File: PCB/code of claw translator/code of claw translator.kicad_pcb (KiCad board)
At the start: 2 copper layers, 43 parts, among them J1 Conn_01x20_Socket, J10 Conn_01x01_Socket, J11 Conn_01x03_Socket, J12 Conn_01x01_Socket, J13 Conn_01x01_Socket, J14 Conn_01x01_Socket, J15 Conn_01x01_Socket, J16 Conn_01x01_Socket, J17 Conn_01x01_Socket, J18 Conn_01x01_Socket, J19 Conn_01x01_Socket, J2 Conn_01x20_Socket, J20 Conn_01x01_Socket, J21 Conn_01x01_Socket, J22 Conn_01x01_Socket, J23 Conn_01x01_Socket, J24 Conn_01x01_Socket, J25 Conn_01x01_Socket, J26 Conn_01x01_Socket, J27 Conn_01x01_Socket, J3 Conn_01x14_Socket, J32 Conn_01x01_Socket, J33 Conn_01x01_Socket, J34 Conn_01x01_Socket, J35 Conn_01x01_Socket, J36 Conn_01x01_Socket, J37 Conn_01x01_Socket, J38 Conn_01x01_Socket, J39 Conn_01x01_Socket, J4 Conn_01x08_Socket, J40 Conn_01x01_Socket, J41 Conn_01x01_Socket, J42 Conn_01x01_Socket, J43 Conn_01x01_Socket, J5 Conn_01x08_Socket, J6 Conn_01x06_Socket, J7 Conn_01x01_Socket, J8 Conn_01x01_Socket, J9 Conn_01x01_Socket

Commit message: Finished rough draft of components in PCB. Now need to wire them up.
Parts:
- removed J34, J35, J38, J39, J42, J43: Conn_01x01_Socket, Connector_PinSocket_2.54mm:PinSocket_1x01_P2.54mm_Horizontal
- J6: footprint Connector_PinSocket_2.54mm:PinSocket_1x06_P2.54mm_Horizontal -> Connector_PinSocket_2.54mm:PinSocket_1x06_P2.54mm_Vertical
- moved J7 124.2 mm to (68.2, 77.0)
- moved J25 123.5 mm to (77.9, 153.3)
- moved J24 123.4 mm to (77.9, 148.3)
- moved J8 121.2 mm to (73.9, 77.0)
- moved J27 109.4 mm to (90.9, 153.3)
- moved J26 109.4 mm to (90.9, 148.3)
- moved J9 108.7 mm to (87.7, 82.5)
- moved J10 108.0 mm to (87.7, 88.5)
- moved J11 107.4 mm to (118.0, 60.0)
- moved J23 91.9 mm to (104.0, 153.3)
- moved J22 91.8 mm to (104.0, 148.3)
- moved J18 86.6 mm to (104.0, 136.3)
- moved J19 86.6 mm to (104.0, 141.3)
- moved J21 80.8 mm to (117.0, 153.3)
- moved J20 80.7 mm to (117.0, 148.3)
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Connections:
- J13 pad 1: unconnected-(J13-Pin_1-Pad1) -> B1
- J14 pad 1: B1 -> unconnected-(J14-Pin_1-Pad1)
- J17 pad 1: unconnected-(J17-Pin_1-Pad1) -> A12
- J18 pad 1: A12 -> unconnected-(J18-Pin_1-Pad1)
- J21 pad 1: unconnected-(J21-Pin_1-Pad1) -> B13
- J22 pad 1: B13 -> unconnected-(J22-Pin_1-Pad1)
- J25 pad 1: unconnected-(J25-Pin_1-Pad1) -> A11
- J26 pad 1: A11 -> unconnected-(J26-Pin_1-Pad1)
- J33 pad 1: unconnected-(J33-Pin_1-Pad1) -> A10
- J37 pad 1: unconnected-(J37-Pin_1-Pad1) -> A8
- J41 pad 1: unconnected-(J41-Pin_1-Pad1) -> A9

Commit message: Finished rough PCB routing
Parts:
- moved H4 107.5 mm to (122.5, 152.9)
- moved H3 87.1 mm to (68.9, 152.9)
- moved H2 73.7 mm to (122.5, 51.1)
- moved J10 21.0 mm to (87.7, 109.5)
- moved J7 21.0 mm to (68.2, 98.0)
- moved J8 21.0 mm to (73.9, 98.0)
- moved J9 21.0 mm to (87.7, 103.5)
- moved H1 19.9 mm to (68.9, 51.1)
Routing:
- net B7: track 0.00 -> 117.9 mm, vias 0 -> 4
- net B6: track 0.00 -> 116.1 mm, vias 0 -> 2
- net B13: track 0.00 -> 108.3 mm, vias 0 -> 4
- net B1: track 0.00 -> 92.0 mm, vias 0 -> 4
- net A11: track 0.00 -> 91.3 mm, vias 0 -> 2
- net 3.3V: track 0.00 -> 84.7 mm
- net A12: track 0.00 -> 75.5 mm, vias 0 -> 6
- net B14: track 0.00 -> 67.7 mm, vias 0 -> 4
- net B10: track 0.00 -> 65.8 mm, vias 0 -> 4
- net B15: track 0.00 -> 63.2 mm, vias 0 -> 4
- net 5V: track 0.00 -> 56.6 mm
- net A6: track 0.00 -> 53.7 mm, vias 0 -> 4
- net A5: track 0.00 -> 52.4 mm, vias 0 -> 4
- net A4: track 0.00 -> 51.8 mm, vias 0 -> 2
- net A0: track 0.00 -> 48.6 mm, vias 0 -> 2
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- added copper zone on B.Cu, net GND
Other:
- board outline added: 59.6 x 107.7 mm

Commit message: Added code for a potentiometer to control sensitivity of the microphone, but might not include it in the final design:
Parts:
- added J28: Conn_01x01_Socket, Connector_PinSocket_2.54mm:PinSocket_1x01_P2.54mm_Vertical, F.Cu at (138.4, 73.6)
- added J29: Conn_01x01_Socket, Connector_PinSocket_2.54mm:PinSocket_1x01_P2.54mm_Vertical, F.Cu at (140.5, 68.3)
- added J30: Conn_01x01_Socket, Connector_PinSocket_2.54mm:PinSocket_1x01_P2.54mm_Vertical, F.Cu at (135.7, 65.9)
- added J31: Conn_01x01_Socket, Connector_PinSocket_2.54mm:PinSocket_1x01_P2.54mm_Vertical, F.Cu at (136.8, 61.1)
- J11: value Conn_01x03_Socket -> Conn_01x01_Socket; footprint Connector_PinSocket_2.54mm:PinSocket_1x03_P2.54mm_Vertical -> Connector_PinSocket_2.54mm:PinSocket_1x01_P2.54mm_Vertical
- moved J11 13.9 mm to (131.8, 62.0)
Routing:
- net A0: track 48.6 -> 0.71 mm, vias 2 -> 0
- net 3.3V: track 84.7 -> 72.7 mm
- net GND: track 41.3 -> 38.8 mm, vias 16 -> 15

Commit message: Ready PCB ready to print
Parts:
- removed J11, J28, J29, J30, J31: Conn_01x01_Socket, Connector_PinSocket_2.54mm:PinSocket_1x01_P2.54mm_Vertical
- added H5: MountingHole, MountingHole:MountingHole_3.2mm_M3, F.Cu at (78.9, 54.3)
- added H6: MountingHole, MountingHole:MountingHole_3.2mm_M3, F.Cu at (115.9, 54.3)
- added H7: MountingHole, MountingHole:MountingHole_3.2mm_M3, F.Cu at (115.9, 122.8)
- added H8: MountingHole, MountingHole:MountingHole_3.2mm_M3, F.Cu at (78.9, 122.8)
- moved H1 3.00 mm to (68.9, 48.1)
- moved H2 3.00 mm to (122.5, 48.1)
- moved J6 3.00 mm to (103.8, 47.7)
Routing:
- net B12: track 13.6 -> 16.6 mm
- net B5: track 46.3 -> 49.3 mm
- net A15: track 42.2 -> 45.2 mm
- net 5V: track 56.6 -> 54.9 mm
- net GND: track 38.8 -> 40.2 mm
- net 3.3V: track 72.7 -> 73.6 mm
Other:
- board size 59.6 x 107.7 mm -> 59.6 x 110.7 mm

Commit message: Finally finished PCB, submitted it for manufacturing
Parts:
- moved H5 1.50 mm to (78.9, 55.8)
- moved H6 1.50 mm to (115.9, 55.8)
- moved H7 0.50 mm to (115.9, 123.3)
- moved H8 0.50 mm to (78.9, 123.3)
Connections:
- J8 pad 1: 5V -> 5V_S
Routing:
- net 5V: track 54.9 -> 30.9 mm
- net GND: track 40.2 -> 39.3 mm
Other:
- board text added: "->"
- board text added: "<-"
- board text added: "Backspace"
- board text added: "Black Pill"
- board text added: "Clear"
- board text added: "Click"
- board text added: "Connect with switch"
- board text added: "ILI9341"
- board text added: "MTCH6102"
- board text added: "Period"
- board text added: "Power Converter"
- board text added: "SPH0645LM4H"
- board text added: "Scratch"
- board text added: "Space"
- board text added: "Tap"
- board text added: "Vandar Systems CCT-1"

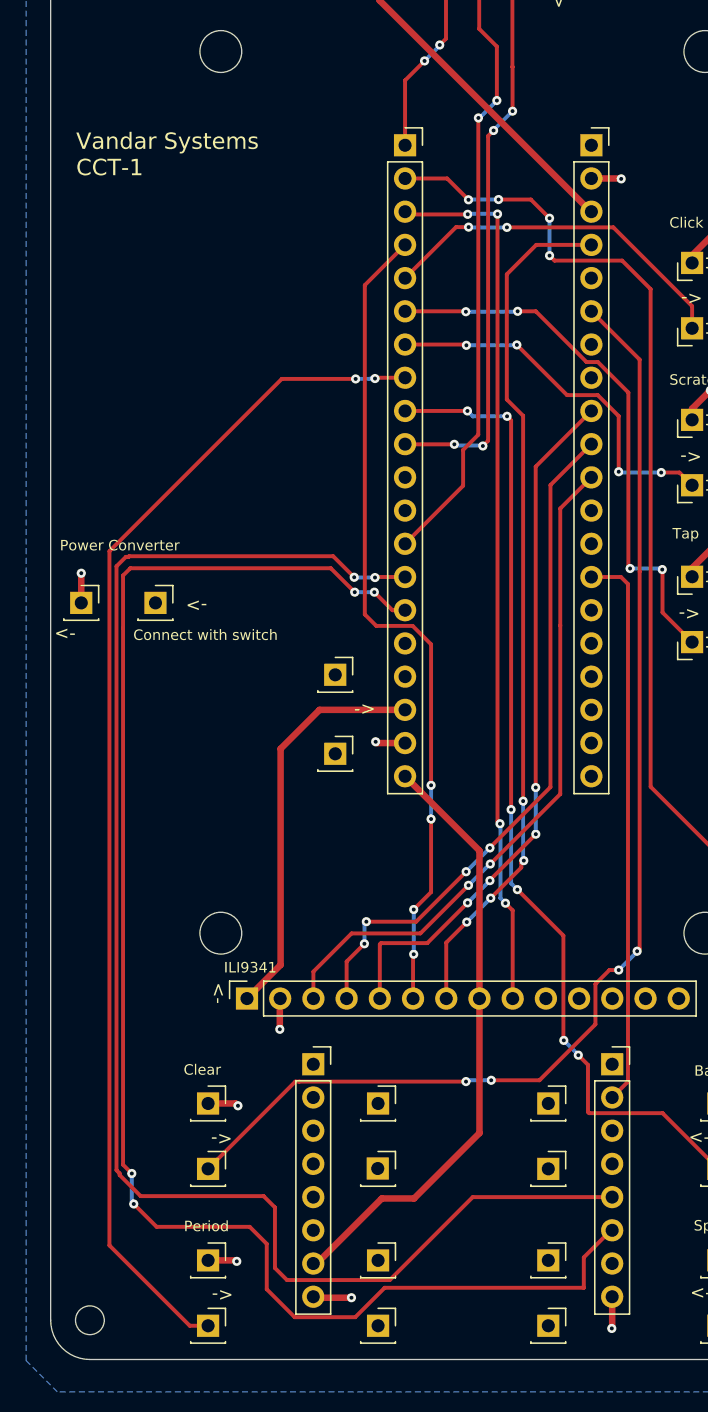
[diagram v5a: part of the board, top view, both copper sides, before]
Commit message: Updated PCB files. Need to update manufacturing files and sent to JLCPCB to manufacture it
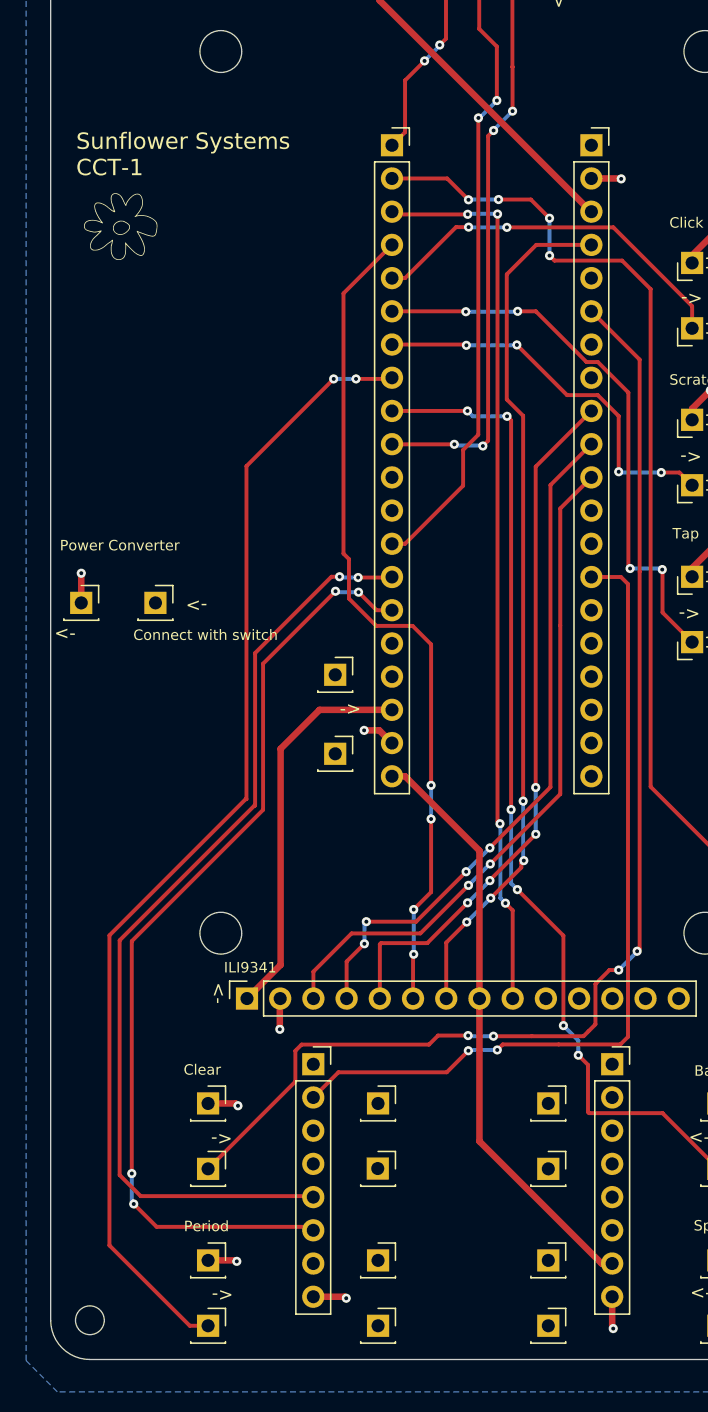
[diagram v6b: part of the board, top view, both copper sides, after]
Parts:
- added ?: LOGO, LOGO, F.Cu at (71.5, 68.9)
- moved J4 22.9 mm to (108.8, 133.3)
- moved J5 22.9 mm to (86.0, 133.3)
- moved J1 1.00 mm to (92.0, 63.0)
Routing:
- net B7: track 117.9 -> 72.9 mm
- net B6: track 116.1 -> 72.7 mm
- net A1: track 42.8 -> 63.6 mm, vias 0 -> 2
- net A11: track 91.3 -> 88.0 mm
- net B1: track 92.0 -> 93.4 mm
- net 3.3V: track 73.6 -> 72.4 mm
- net A12: track 75.5 -> 76.5 mm
- net B5: track 49.3 -> 50.3 mm
- net A15: track 45.2 -> 46.2 mm
- net B14: track 67.7 -> 68.7 mm
- net B13: track 108.3 -> 109.3 mm
- net A9: track 42.2 -> 43.2 mm
- net A8: track 27.8 -> 28.8 mm
- net A10: track 29.1 -> 30.1 mm
- net 5V: track 30.9 -> 29.9 mm
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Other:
- board text added: "Sunflower Systems CCT-1"
- board text removed: "Vandar Systems CCT-1"
